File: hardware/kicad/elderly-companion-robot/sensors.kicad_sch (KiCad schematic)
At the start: 10 parts, among them J5 US_Front, J6 US_Back, J7 US_Left, J8 US_Right, U6 MPU-6050, U7 SSD1306_OLED

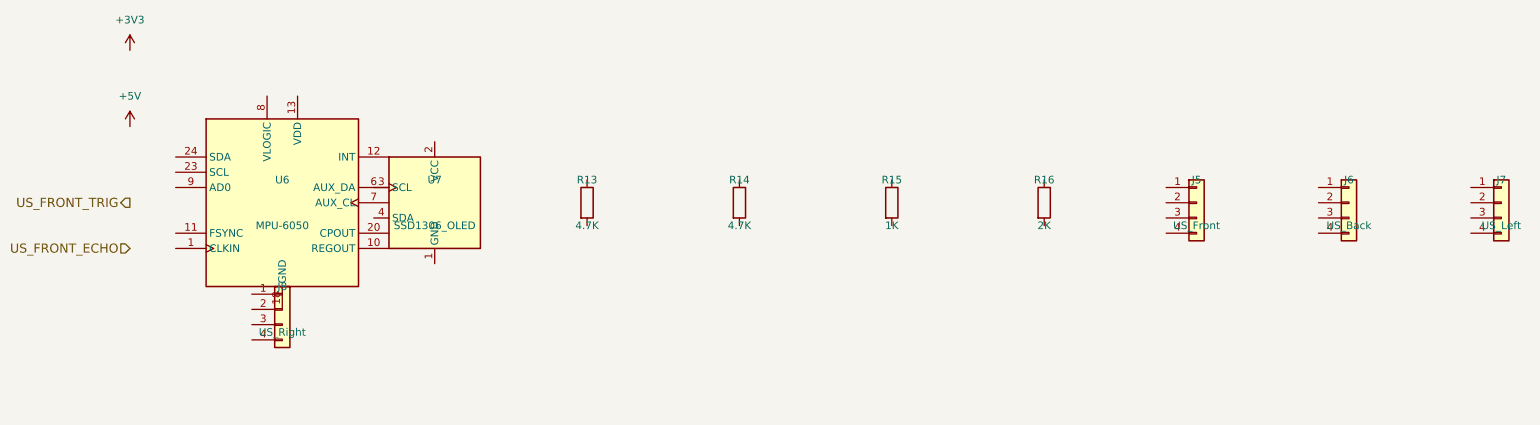
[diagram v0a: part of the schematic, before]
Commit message: Add net labels and signal connections across all schematic sheets
- MCU Core: Added net labels at all ESP32-S3 GPIO pin positions
  (I2C, I2S, motor, servo, IR, UART, ultrasonic signals)
- Added hierarchical labels for US_LEFT/RIGHT_TRIG/ECHO
- Remapped I2C_SCL to GPIO2 (GPIO22 not on WROOM-1 module)
- Remapped SERVO_PAN to GPIO42 (GPIO44 not available)
- Motor Driver: Added net labels at L298N input/output pins
- Sensors: Added I2C labels at MPU-6050 and SSD1306 pin positions
- Audio: Added I2S labels at MAX98357A and INMP441 connector
- Camera/Dock: Added UART, SIM_PWRKEY, servo, IR labels at SIM800C
- Added power symbols (+3V3, +5V, GND, +4V) across all sheets
- Boot circuit wiring started (EN pull-up, GPIO0 connections)
- ERC: 446 violations (mostly unconnected labels/pins - need wires)

Co-Authored-By: Claude Opus 4.7 <noreply@anthropic.com>
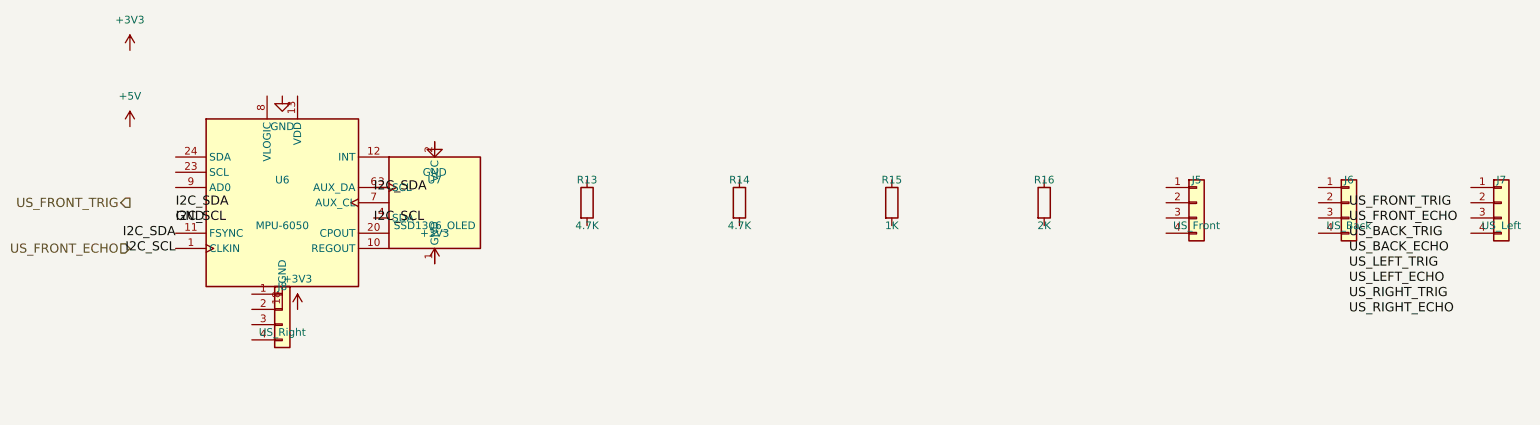
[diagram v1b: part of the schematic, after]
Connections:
- net +3V3: now also U7.1 (GND)
- net GND: now also U6.1 (CLKIN), U7.2 (VCC), U7.4 (SDA)
- net I2C_SDA: now also U6.11 (FSYNC), U7.3 (SCL)
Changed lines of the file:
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@@
 	(version 20250114)
 	(generator "eeschema")
+	(generator_version "9.0")
 	(paper "A4")
 	(symbol
@@
 		(effects (font (size 1.524 1.524)))
 	)
+	(label "I2C_SDA"
+		(at 33.02 50.8 0)
+		(effects (font (size 1.524 1.524)))
+	)
+	(label "I2C_SCL"
+		(at 33.02 53.34 0)
+		(effects (font (size 1.524 1.524)))
+	)
+	(label "US_FRONT_TRIG"
+		(at 228.6 50.8 0)
+		(effects (font (size 1.524 1.524)))
+	)
+	(label "US_FRONT_ECHO"
+		(at 228.6 53.34 0)
+		(effects (font (size 1.524 1.524)))
+	)
+	(label "US_BACK_TRIG"
+		(at 228.6 55.88 0)
+		(effects (font (size 1.524 1.524)))
+	)
+	(label "US_BACK_ECHO"
+		(at 228.6 58.42 0)
+		(effects (font (size 1.524 1.524)))
+	)
+	(label "US_LEFT_TRIG"
+		(at 228.6 60.96 0)
+		(effects (font (size 1.524 1.524)))
+	)
+	(label "US_LEFT_ECHO"
+		(at 228.6 63.5 0)
+		(effects (font (size 1.524 1.524)))
+	)
+	(label "US_RIGHT_TRIG"
+		(at 228.6 66.04 0)
+		(effects (font (size 1.524 1.524)))
+	)
+	(label "US_RIGHT_ECHO"
+		(at 228.6 68.58 0)
+		(effects (font (size 1.524 1.524)))
+	)
+	(label "I2C_SDA"
+		(at 33.02 55.88 180)
+		(effects (font (size 1.524 1.524)))
+	)
+	(label "I2C_SCL"
+		(at 33.02 58.42 180)
+		(effects (font (size 1.524 1.524)))
+	)
+	(label "I2C_SDA"
+		(at 66.04 48.26 0)
+		(effects (font (size 1.524 1.524)))
+	)
+	(label "I2C_SCL"
+		(at 66.04 53.34 0)
+		(effects (font (size 1.524 1.524)))
+	)
+	(symbol
+		(lib_id "power:+3V3")
+		(at 53.34 68.58 0)
+		(unit 1)
+		(exclude_from_sim no)
+		(in_bom yes)
+		(on_board yes)
+		(dnp no)
+		(property "Reference" "#PWR6dc5"
+			(at 53.34 62.23 0)
+			(effects (font (size 1.27 1.27)) (hide yes))
+		)
+		(property "Value" "+3V3"
+			(at 53.34 63.5 0)
+			(effects (font (size 1.27 1.27)))
+		)
+		(property "Footprint" ""
+			(at 53.34 68.58 0)
+			(effects (font (size 1.27 1.27)) (hide yes))
+		)
+		(property "Datasheet" "~"
+			(at 53.34 68.58 0)
+			(effects (font (size 1.27 1.27)) (hide yes))
+		)
+		(instances
+			(project "elderly-companion-robot"
+				(path "/283ca26f-9a41-46d2-95bb-5d1a536a2b24"
+					(reference "#PWR6dc5") (unit 1)
+				)
+			)
+		)
+	)
+	(symbol
+		(lib_id "power:GND")
+		(at 50.8 33.02 0)
+		(unit 1)
+		(exclude_from_sim no)
+		(in_bom yes)
+		(on_board yes)
+		(dnp no)
+		(property "Reference" "#PWRc250"
+			(at 50.8 39.37 0)
+			(effects (font (size 1.27 1.27)) (hide yes))
+		)
+		(property "Value" "GND"
+			(at 50.8 38.1 0)
+			(effects (font (size 1.27 1.27)))
+		)
+		(property "Footprint" ""
+			(at 50.8 33.02 0)
+			(effects (font (size 1.27 1.27)) (hide yes))
+		)
+		(property "Datasheet" "~"
+			(at 50.8 33.02 0)
+			(effects (font (size 1.27 1.27)) (hide yes))
+		)
+		(instances
+			(project "elderly-companion-robot"
+				(path "/81283502-27c4-4593-b87b-c992e6ede747"
+					(reference "#PWRc250") (unit 1)
+				)
+			)
+		)
+	)
+	(label "GND"
+		(at 33.02 53.34 0)
+		(effects (font (size 1.524 1.524)))
+	)
+	(symbol
+		(lib_id "power:+3V3")
+		(at 76.2 60.96 0)
+		(unit 1)
+		(exclude_from_sim no)
+		(in_bom yes)
+		(on_board yes)
+		(dnp no)
+		(property "Reference" "#PWR71c8"
+			(at 76.2 54.61 0)
+			(effects (font (size 1.27 1.27)) (hide yes))
+		)
+		(property "Value" "+3V3"
+			(at 76.2 55.88 0)
+			(effects (font (size 1.27 1.27)))
+		)
+		(property "Footprint" ""
+			(at 76.2 60.96 0)
+			(effects (font (size 1.27 1.27)) (hide yes))
+		)
+		(property "Datasheet" "~"
+			(at 76.2 60.96 0)
+			(effects (font (size 1.27 1.27)) (hide yes))
+		)
+		(instances
+			(project "elderly-companion-robot"
+				(path "/2103488b-35f4-4549-a884-6fbd35386922"
+					(reference "#PWR71c8") (unit 1)
+				)
+			)
+		)
+	)
+	(symbol
+		(lib_id "power:GND")
+		(at 76.2 40.64 0)
+		(unit 1)
+		(exclude_from_sim no)
+		(in_bom yes)
+		(on_board yes)
+		(dnp no)
+		(property "Reference" "#PWR325c"
+			(at 76.2 46.99 0)
+			(effects (font (size 1.27 1.27)) (hide yes))
+		)
+		(property "Value" "GND"
+			(at 76.2 45.72 0)
+			(effects (font (size 1.27 1.27)))
+		)
+		(property "Footprint" ""
+			(at 76.2 40.64 0)
+			(effects (font (size 1.27 1.27)) (hide yes))
+		)
+		(property "Datasheet" "~"
+			(at 76.2 40.64 0)
+			(effects (font (size 1.27 1.27)) (hide yes))
+		)
+		(instances
+			(project "elderly-companion-robot"
+				(path "/d9b3e4cb-0194-49a0-9adc-b000a62645e2"
+					(reference "#PWR325c") (unit 1)
+				)
+			)
+		)
+	)
 	(sheet_instances
